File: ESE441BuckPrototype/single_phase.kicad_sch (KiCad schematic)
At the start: 0 parts

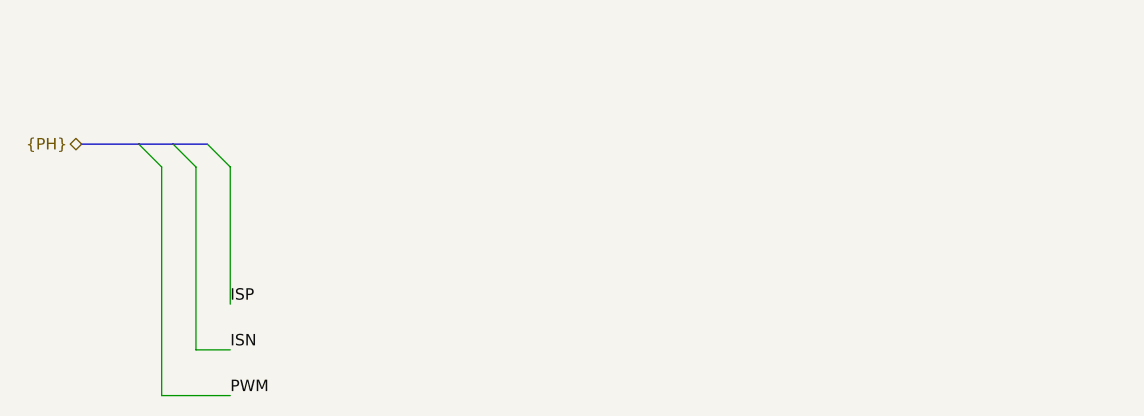
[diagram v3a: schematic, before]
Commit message: Implement basic phase layout
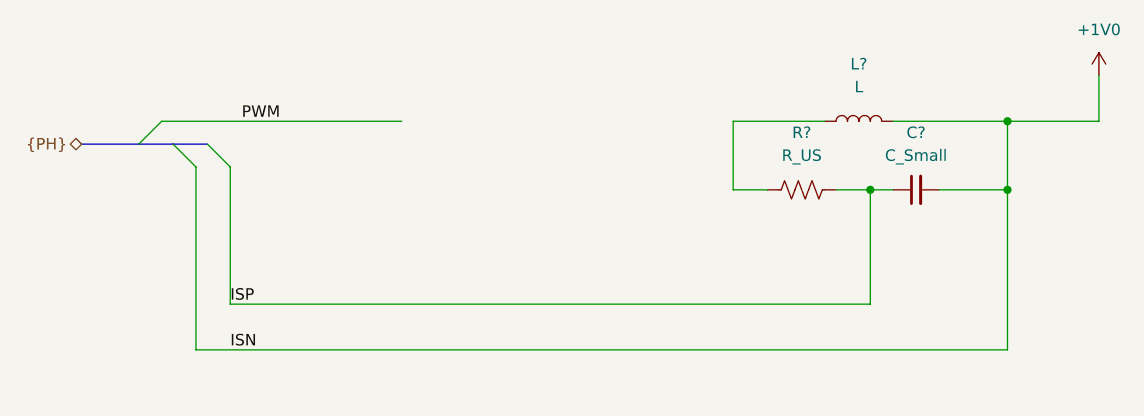
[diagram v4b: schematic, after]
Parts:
- added C?: C_Small, symbol Device:C_Small
- added L?: L, symbol Device:L
- added R?: R_US, symbol Device:R_US
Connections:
- net ISP: now also C?.1, R?.2
- new net: L?.1, R?.1
- new net +1V0: C?.2, L?.2
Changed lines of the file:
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@@
 (kicad_sch (version 20211123) (generator eeschema)
   (paper "A4")
-  (bus_entry (at 66.04 36.83) (size 2.54 2.54)
+  (junction (at 147.32 41.91) (diameter 0) (color 0 0 0 0)
+  )
+  (junction (at 162.56 34.29) (diameter 0) (color 0 0 0 0)
+  )
+  (junction (at 162.56 41.91) (diameter 0) (color 0 0 0 0)
+  )
+  (bus_entry (at 66.04 36.83) (size 2.54 -2.54)
     (stroke (width 0) (type default) (color 0 0 0 0))
   )
@@
     (stroke (width 0) (type default) (color 0 0 0 0))
   )
+  (wire (pts (xy 149.86 34.29) (xy 162.56 34.29))
+    (stroke (width 0) (type default) (color 0 0 0 0))
+  )
+  (wire (pts (xy 162.56 34.29) (xy 172.72 34.29))
+    (stroke (width 0) (type default) (color 0 0 0 0))
+  )
   (bus (pts (xy 59.69 36.83) (xy 66.04 36.83))
     (stroke (width 0) (type default) (color 0 0 0 0))
   )
-  (wire (pts (xy 72.39 59.69) (xy 76.2 59.69))
+  (wire (pts (xy 142.24 34.29) (xy 132.08 34.29))
+    (stroke (width 0) (type default) (color 0 0 0 0))
+  )
+  (wire (pts (xy 172.72 29.21) (xy 172.72 34.29))
+    (stroke (width 0) (type default) (color 0 0 0 0))
+  )
+  (wire (pts (xy 72.39 59.69) (xy 162.56 59.69))
+    (stroke (width 0) (type default) (color 0 0 0 0))
+  )
+  (wire (pts (xy 132.08 34.29) (xy 132.08 41.91))
+    (stroke (width 0) (type default) (color 0 0 0 0))
+  )
+  (wire (pts (xy 147.32 41.91) (xy 149.86 41.91))
+    (stroke (width 0) (type default) (color 0 0 0 0))
+  )
+  (wire (pts (xy 162.56 59.69) (xy 162.56 41.91))
+    (stroke (width 0) (type default) (color 0 0 0 0))
+  )
+  (wire (pts (xy 162.56 34.29) (xy 162.56 41.91))
     (stroke (width 0) (type default) (color 0 0 0 0))
   )
   (wire (pts (xy 76.2 39.37) (xy 76.2 54.61))
+    (stroke (width 0) (type default) (color 0 0 0 0))
+  )
+  (wire (pts (xy 147.32 54.61) (xy 76.2 54.61))
+    (stroke (width 0) (type default) (color 0 0 0 0))
+  )
+  (wire (pts (xy 132.08 41.91) (xy 135.89 41.91))
+    (stroke (width 0) (type default) (color 0 0 0 0))
+  )
+  (wire (pts (xy 162.56 41.91) (xy 154.94 41.91))
+    (stroke (width 0) (type default) (color 0 0 0 0))
+  )
+  (wire (pts (xy 147.32 41.91) (xy 147.32 54.61))
     (stroke (width 0) (type default) (color 0 0 0 0))
   )
@@
     (stroke (width 0) (type default) (color 0 0 0 0))
   )
-  (wire (pts (xy 68.58 39.37) (xy 68.58 64.77))
+  (wire (pts (xy 143.51 41.91) (xy 147.32 41.91))
     (stroke (width 0) (type default) (color 0 0 0 0))
   )
-  (wire (pts (xy 68.58 64.77) (xy 76.2 64.77))
+  (wire (pts (xy 68.58 34.29) (xy 95.25 34.29))
     (stroke (width 0) (type default) (color 0 0 0 0))
   )
-  (label "PWM" (at 76.2 64.77 0)
+  (label "PWM" (at 77.47 34.29 0)
     (effects (font (size 1.27 1.27)) (justify left bottom))
   )
@@
     (effects (font (size 1.27 1.27)) (justify right))
   )
+  (symbol (lib_id "Device:R_US") (at 139.7 41.91 90) (unit 1)
+    (in_bom yes) (on_board yes) (fields_autoplaced)
+    (property "Reference" "R?" (id 0) (at 139.7 35.56 90))
+    (property "Value" "R_US" (id 1) (at 139.7 38.1 90))
+    (property "Footprint" "" (id 2) (at 139.954 40.894 90)
+      (effects (font (size 1.27 1.27)) hide)
+    )
+    (property "Datasheet" "~" (id 3) (at 139.7 41.91 0)
+      (effects (font (size 1.27 1.27)) hide)
+    )
+    (pin "1")
+    (pin "2")
+  )
+  (symbol (lib_id "Device:L") (at 146.05 34.29 90) (unit 1)
+    (in_bom yes) (on_board yes) (fields_autoplaced)
+    (property "Reference" "L?" (id 0) (at 146.05 27.94 90))
+    (property "Value" "L" (id 1) (at 146.05 30.48 90))
+    (property "Footprint" "" (id 2) (at 146.05 34.29 0)
+      (effects (font (size 1.27 1.27)) hide)
+    )
+    (property "Datasheet" "~" (id 3) (at 146.05 34.29 0)
+      (effects (font (size 1.27 1.27)) hide)
+    )
+    (pin "1")
+    (pin "2")
+  )
+  (symbol (lib_id "Device:C_Small") (at 152.4 41.91 90) (unit 1)
+    (in_bom yes) (on_board yes) (fields_autoplaced)
+    (property "Reference" "C?" (id 0) (at 152.4063 35.56 90))
+    (property "Value" "C_Small" (id 1) (at 152.4063 38.1 90))
+    (property "Footprint" "" (id 2) (at 152.4 41.91 0)
+      (effects (font (size 1.27 1.27)) hide)
+    )
+    (property "Datasheet" "~" (id 3) (at 152.4 41.91 0)
+      (effects (font (size 1.27 1.27)) hide)
+    )
+    (pin "1")
+    (pin "2")
+  )
+  (symbol (lib_id "power:+1V0") (at 172.72 29.21 0) (unit 1)
+    (in_bom yes) (on_board yes) (fields_autoplaced)
+    (property "Reference" "#PWR?" (id 0) (at 172.72 33.02 0)
+      (effects (font (size 1.27 1.27)) hide)
+    )
+    (property "Value" "+1V0" (id 1) (at 172.72 24.13 0))
+    (property "Footprint" "" (id 2) (at 172.72 29.21 0)
+      (effects (font (size 1.27 1.27)) hide)
+    )
+    (property "Datasheet" "" (id 3) (at 172.72 29.21 0)
+      (effects (font (size 1.27 1.27)) hide)
+    )
+    (pin "1")
+  )
 )

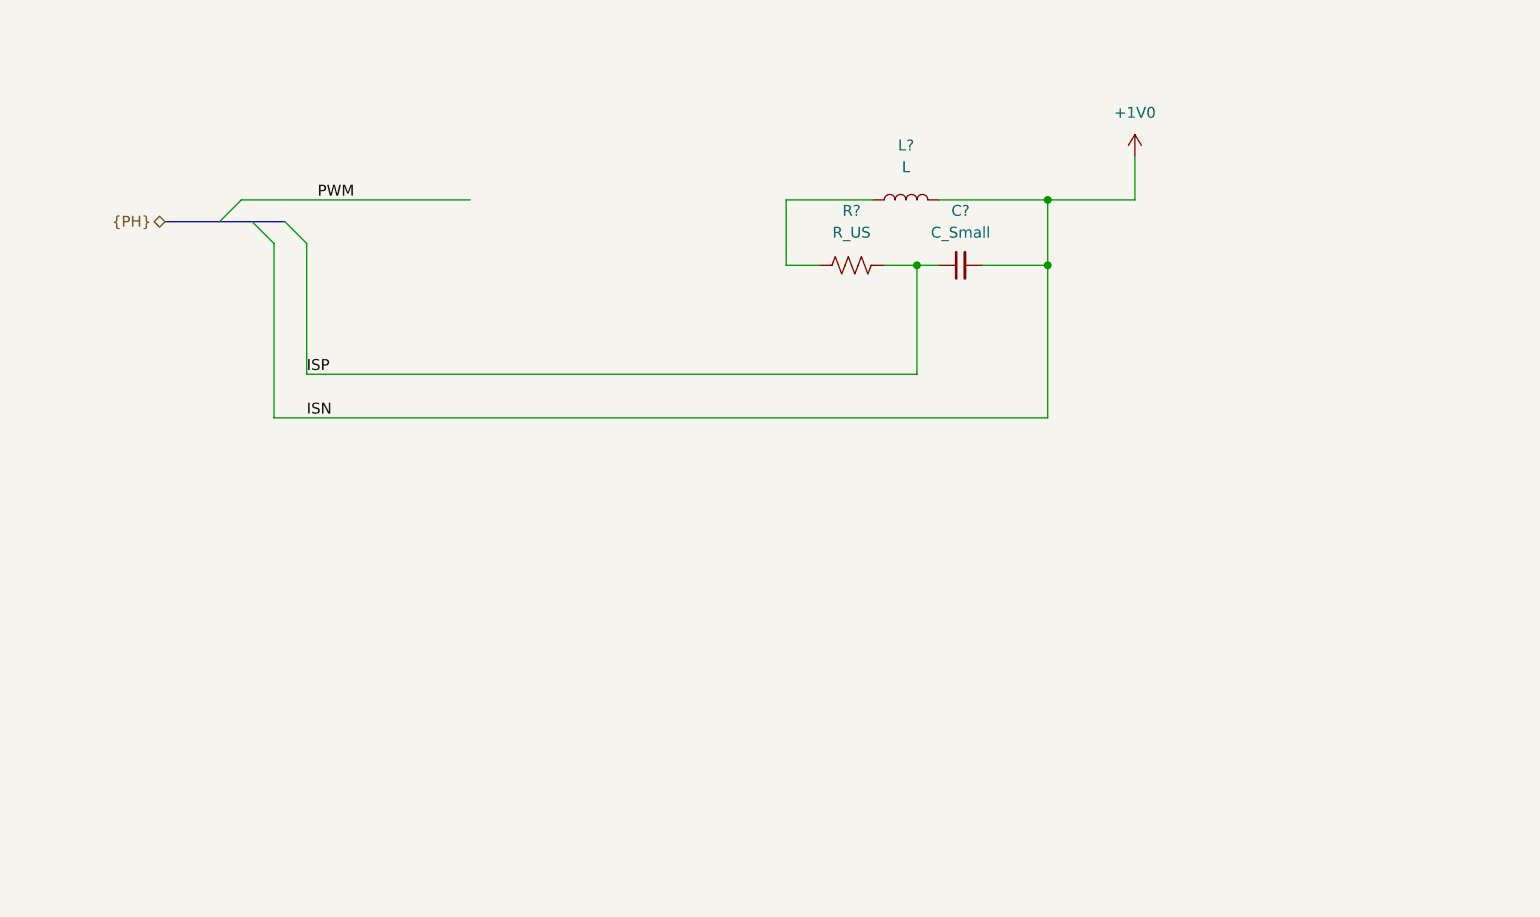
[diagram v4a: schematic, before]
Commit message: Add SIC645 half H-bridge
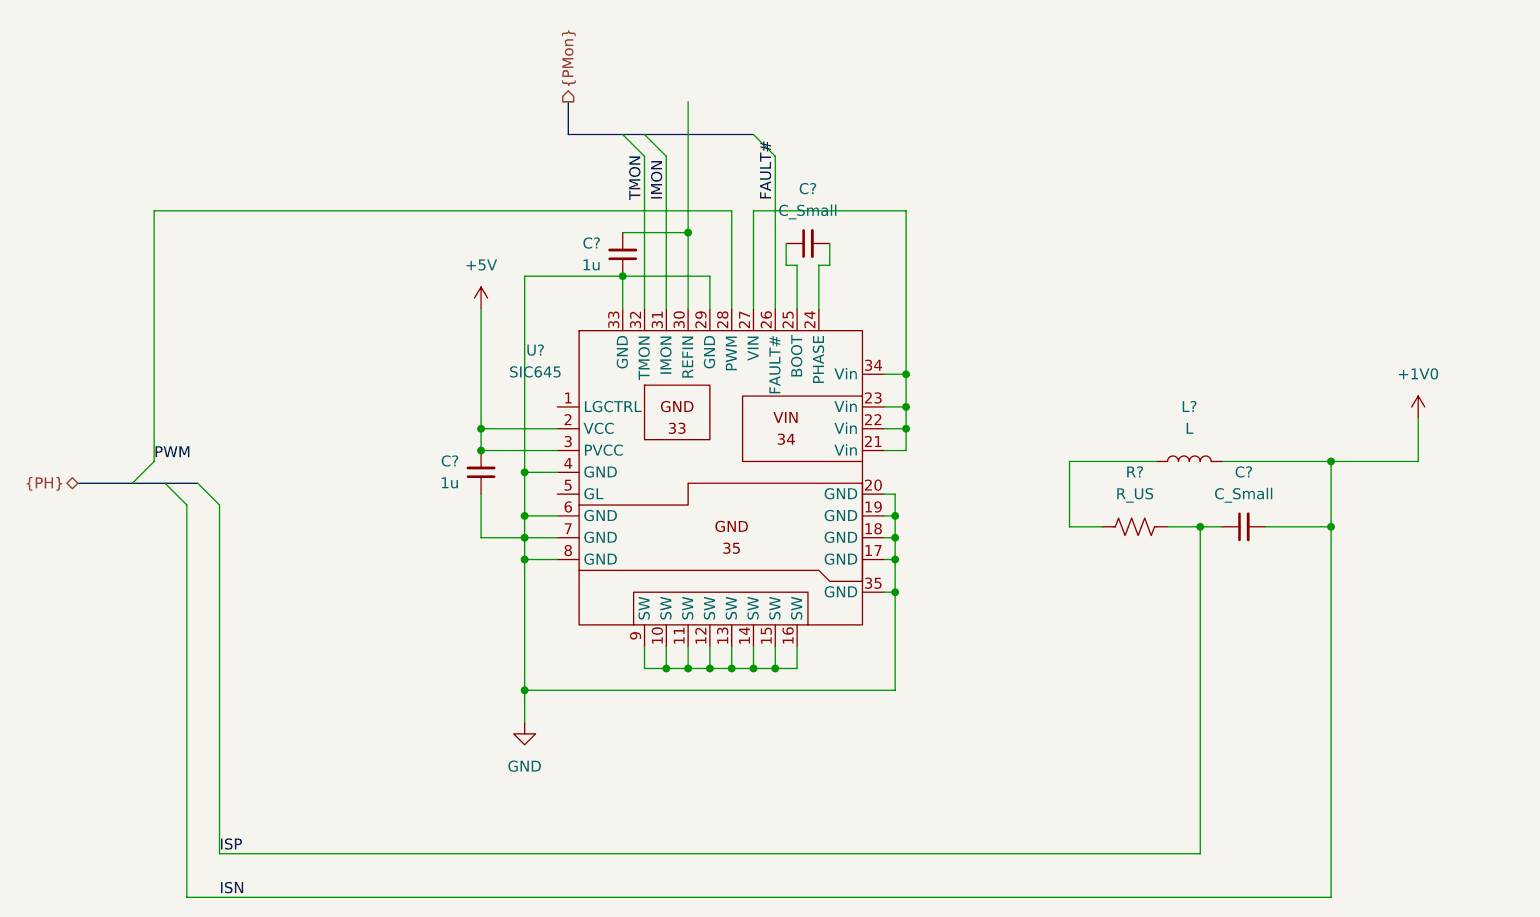
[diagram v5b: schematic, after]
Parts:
- added C?: C_Small, Capacitor_SMD:C_0603_1608Metric, symbol Device:C_Small
- added C? (x2): 1u, Capacitor_SMD:C_0603_1608Metric, symbol Device:C_Small
- added U?: SIC645, symbol CustomPartsLibrary:SIC645
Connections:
- net PWM: now also U?.28 (PWM)
- new net: C?.1, U?.25 (BOOT)
- new net: C?.2, U?.24 (PHASE)
- new net: U?.10 (SW), U?.11 (SW), U?.12 (SW), U?.13 (SW), U?.14 (SW), U?.15 (SW), U?.16 (SW), U?.9 (SW)
- new net: U?.21 (Vin), U?.22 (Vin), U?.23 (Vin), U?.27 (VIN), U?.34 (Vin)
- new net: C?.2, U?.30 (REFIN)
- new net +5V: C?.2, U?.2 (VCC), U?.3 (PVCC)
- new net FAULT#: U?.26 (FAULT#)
- new net GND: C?.1, C?.1, U?.17 (GND), U?.18 (GND), U?.19 (GND), U?.20 (GND), U?.29 (GND), U?.33 (GND), U?.35 (GND), U?.4 (GND), U?.6 (GND), U?.7 (GND), U?.8 (GND)
- new net IMON: U?.31 (IMON)
- new net TMON: U?.32 (TMON)
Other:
- moved on the sheet: C?, L?, R?

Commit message: Add values for current measuring capacitor
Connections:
- net at L?.1, R?.1: now also U?.10 (SW), U?.11 (SW), U?.12 (SW), U?.13 (SW), U?.14 (SW), U?.15 (SW), U?.16 (SW), U?.9 (SW)
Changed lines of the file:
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@@
   (junction (at 101.6 76.2) (diameter 0) (color 0 0 0 0)
   )
+  (junction (at 165.1 72.39) (diameter 0) (color 0 0 0 0)
+  )
   (junction (at 101.6 66.04) (diameter 0) (color 0 0 0 0)
   )
@@
   (junction (at 118.11 88.9) (diameter 0) (color 0 0 0 0)
   )
+  (junction (at 133.35 88.9) (diameter 0) (color 0 0 0 0)
+  )
   (junction (at 144.78 73.66) (diameter 0) (color 0 0 0 0)
   )
@@
     (stroke (width 0) (type default) (color 0 0 0 0))
   )
+  (wire (pts (xy 165.1 88.9) (xy 133.35 88.9))
+    (stroke (width 0) (type default) (color 0 0 0 0))
+  )
   (wire (pts (xy 144.78 71.12) (xy 144.78 73.66))
     (stroke (width 0) (type default) (color 0 0 0 0))
@@
     (stroke (width 0) (type default) (color 0 0 0 0))
   )
+  (wire (pts (xy 165.1 72.39) (xy 165.1 88.9))
+    (stroke (width 0) (type default) (color 0 0 0 0))
+  )

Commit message: Values for current measuring network
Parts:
- added C?: C_Small, Capacitor_SMD:C_0603_1608Metric, symbol Device:C_Small
- C?: value C_Small -> 47n
- R?: value R_US -> 11k
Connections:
- net +1V0: now also C?.2
- new net GNDPWR: C?.1
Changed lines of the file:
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@@
   (junction (at 120.65 38.1) (diameter 0) (color 0 0 0 0)
   )
+  (junction (at 205.74 64.77) (diameter 0) (color 0 0 0 0)
+  )
   (junction (at 144.78 71.12) (diameter 0) (color 0 0 0 0)
   )
@@
     (stroke (width 0) (type default) (color 0 0 0 0))
   )
+  (wire (pts (xy 205.74 76.2) (xy 205.74 83.82))
+    (stroke (width 0) (type default) (color 0 0 0 0))
+  )
   (wire (pts (xy 58.42 64.77) (xy 58.42 35.56))
     (stroke (width 0) (type default) (color 0 0 0 0))
@@
   )
   (wire (pts (xy 133.35 46.99) (xy 133.35 41.91))
+    (stroke (width 0) (type default) (color 0 0 0 0))
+  )
+  (wire (pts (xy 205.74 71.12) (xy 205.74 64.77))
     (stroke (width 0) (type default) (color 0 0 0 0))
   )
@@
     (effects (font (size 1.27 1.27)) (justify left))
   )
+  (symbol (lib_id "Device:C_Small") (at 205.74 73.66 180) (unit 1)
+    (in_bom yes) (on_board yes) (fields_autoplaced)
+    (property "Reference" "C?" (id 0) (at 208.28 72.3835 0)
+      (effects (font (size 1.27 1.27)) (justify right))
+    )
+    (property "Value" "C_Small" (id 1) (at 208.28 74.9235 0)
+      (effects (font (size 1.27 1.27)) (justify right))
+    )
+    (property "Footprint" "Capacitor_SMD:C_0603_1608Metric" (id 2) (at 205.74 73.66 0)
+      (effects (font (size 1.27 1.27)) hide)
+    )
+    (property "Datasheet" "~" (id 3) (at 205.74 73.66 0)
+      (effects (font (size 1.27 1.27)) hide)
+    )
+    (pin "1")
+    (pin "2")
+  )
   (symbol (lib_id "power:GND") (at 101.6 95.25 0) (unit 1)
     (in_bom yes) (on_board yes) (fields_autoplaced)
@@
     (in_bom yes) (on_board yes) (fields_autoplaced)
     (property "Reference" "R?" (id 0) (at 172.72 66.04 90))
-    (property "Value" "R_US" (id 1) (at 172.72 68.58 90))
+    (property "Value" "11k" (id 1) (at 172.72 68.58 90))
     (property "Footprint" "" (id 2) (at 172.974 71.374 90)
       (effects (font (size 1.27 1.27)) hide)
@@
     (in_bom yes) (on_board yes) (fields_autoplaced)
     (property "Reference" "C?" (id 0) (at 185.4263 66.04 90))
-    (property "Value" "C_Small" (id 1) (at 185.4263 68.58 90))
+    (property "Value" "47n" (id 1) (at 185.4263 68.58 90))
     (property "Footprint" "" (id 2) (at 185.42 72.39 0)
       (effects (font (size 1.27 1.27)) hide)
@@
     (pin "9")
   )
+  (symbol (lib_id "power:GNDPWR") (at 205.74 83.82 0) (unit 1)
+    (in_bom yes) (on_board yes) (fields_autoplaced)
+    (property "Reference" "#PWR?" (id 0) (at 205.74 88.9 0)
+      (effects (font (size 1.27 1.27)) hide)
+    )
+    (property "Value" "GNDPWR" (id 1) (at 205.613 88.9 0))
+    (property "Footprint" "" (id 2) (at 205.74 85.09 0)
+      (effects (font (size 1.27 1.27)) hide)
+    )
+    (property "Datasheet" "" (id 3) (at 205.74 85.09 0)
+      (effects (font (size 1.27 1.27)) hide)
+    )
+    (pin "1")
+  )
   (symbol (lib_id "Device:C_Small") (at 113.03 40.64 0) (mirror x) (unit 1)
